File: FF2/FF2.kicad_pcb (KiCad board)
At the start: 2 copper layers, 140 x 140 mm, 80 parts, among them J1 AVR-ISP-6, SW1 RESET, SW2 BOOT, U1 ATmega328P-AU, Y1 16MHz

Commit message: updated switches footprints lib, start of placement on board
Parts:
- moved MX15 255.2 mm to (151.6, 132.1)
- moved DOB1 249.9 mm to (171.0, 132.1)
- moved H3 239.2 mm to (103.2, 156.0)
- moved MX20 238.4 mm to (190.5, 113.0)
- moved MX21 233.9 mm to (190.5, 132.2)
- moved H4 226.7 mm to (200.3, 156.0)
- moved MX19 220.7 mm to (190.5, 93.8)
- moved MX5 217.3 mm to (113.2, 132.1)
- moved MX10 216.6 mm to (132.4, 132.1)
- moved MX18 210.9 mm to (190.5, 74.6)
- moved MX17 204.9 mm to (190.4, 50.8)
- moved MX14 204.4 mm to (151.6, 112.9)
- moved MX3 181.4 mm to (113.2, 93.7)
- moved MX9 177.3 mm to (132.4, 112.9)
- moved MX4 156.6 mm to (113.2, 112.9)
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
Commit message: more component placement on the pcb
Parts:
- C1, C2, C3, C4, D1, D10, D11, D12, D13, D14, D15, D16, D17, D18, D19, D2, D20, D21, D3, D4, D5, D6, D7, D8, D9, DBA1, DBB1, DBC1, DBD1, DBP1, DM1, DM2, DR1, DR2, DZ1, DZ2, J1, R1, R2, R3, R4, R5, R6, R7, SW1, SW2, U1, Y1: moved to B.Cu
- moved DBP1 208.5 mm to (172.6, 143.3)
- moved D10 196.5 mm to (133.2, 122.5)
- moved DBB1 192.4 mm to (177.3, 143.3)
- moved D5 191.2 mm to (114.1, 122.5)
- moved DBD1 188.3 mm to (172.6, 121.8)
- moved DBA1 187.6 mm to (167.8, 143.3)
- moved D21 184.7 mm to (191.4, 122.7)
- moved DBC1 182.4 mm to (177.3, 121.8)
- moved DR2 180.5 mm to (176.5, 82.5)
- moved D20 163.6 mm to (191.3, 103.4)
- moved D14 158.4 mm to (152.5, 103.3)
- moved D15 155.0 mm to (152.4, 122.5)
- moved D9 154.2 mm to (133.2, 103.3)
- moved D19 152.7 mm to (191.3, 84.2)
- moved D4 150.6 mm to (114.1, 103.3)
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
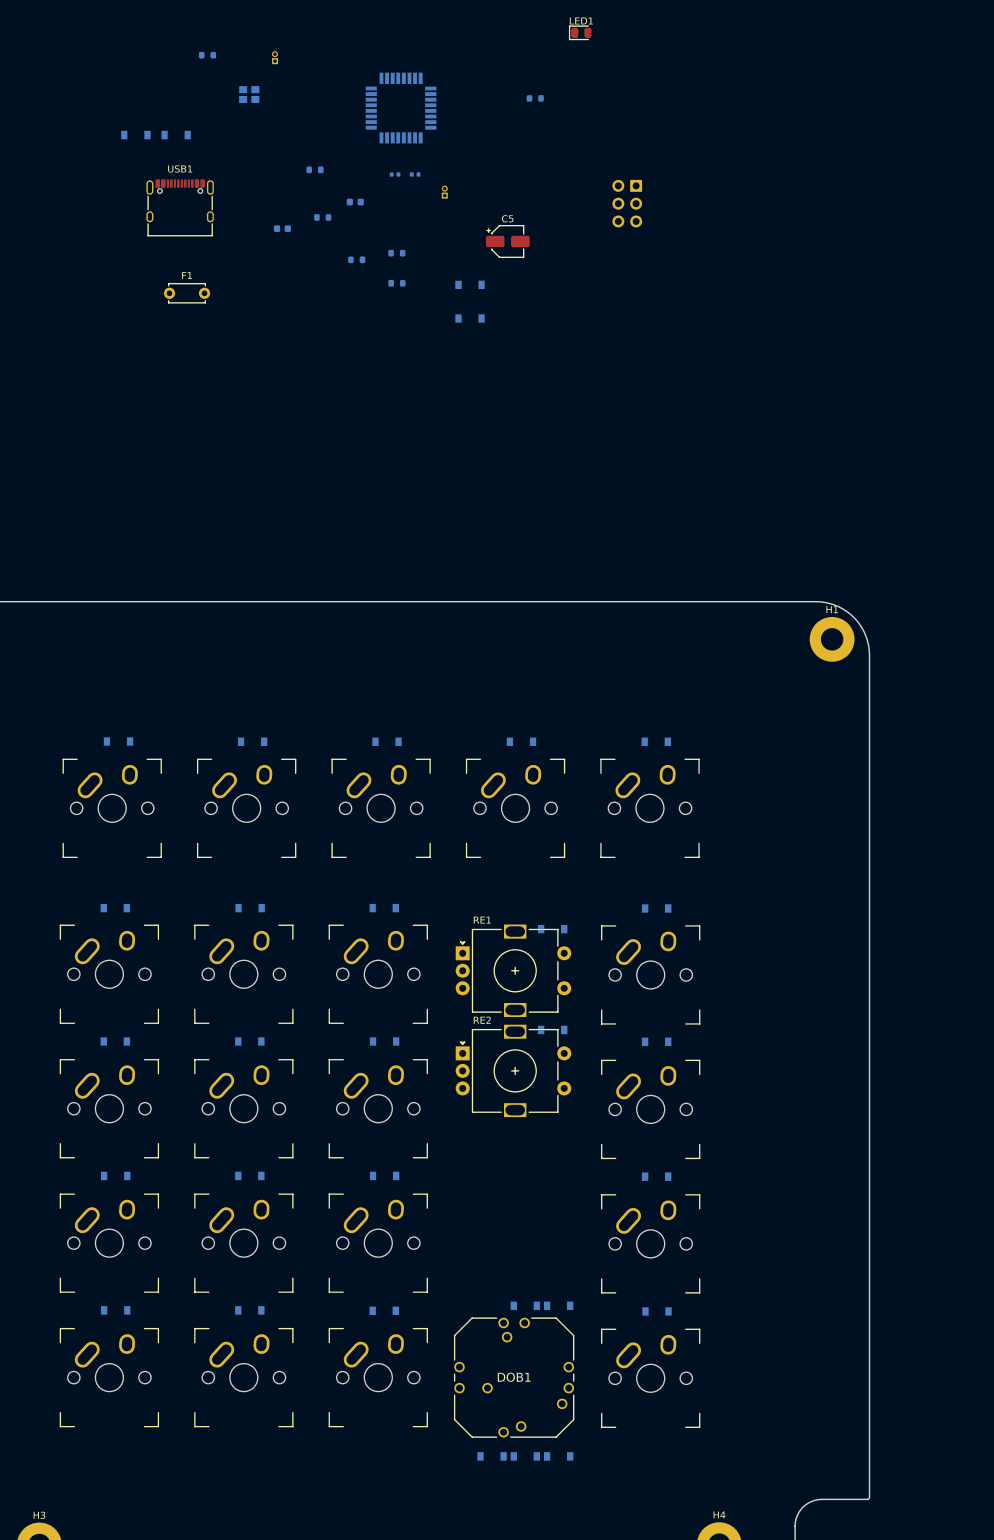
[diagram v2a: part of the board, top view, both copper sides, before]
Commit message: more routing, only dobber and 2-way missing
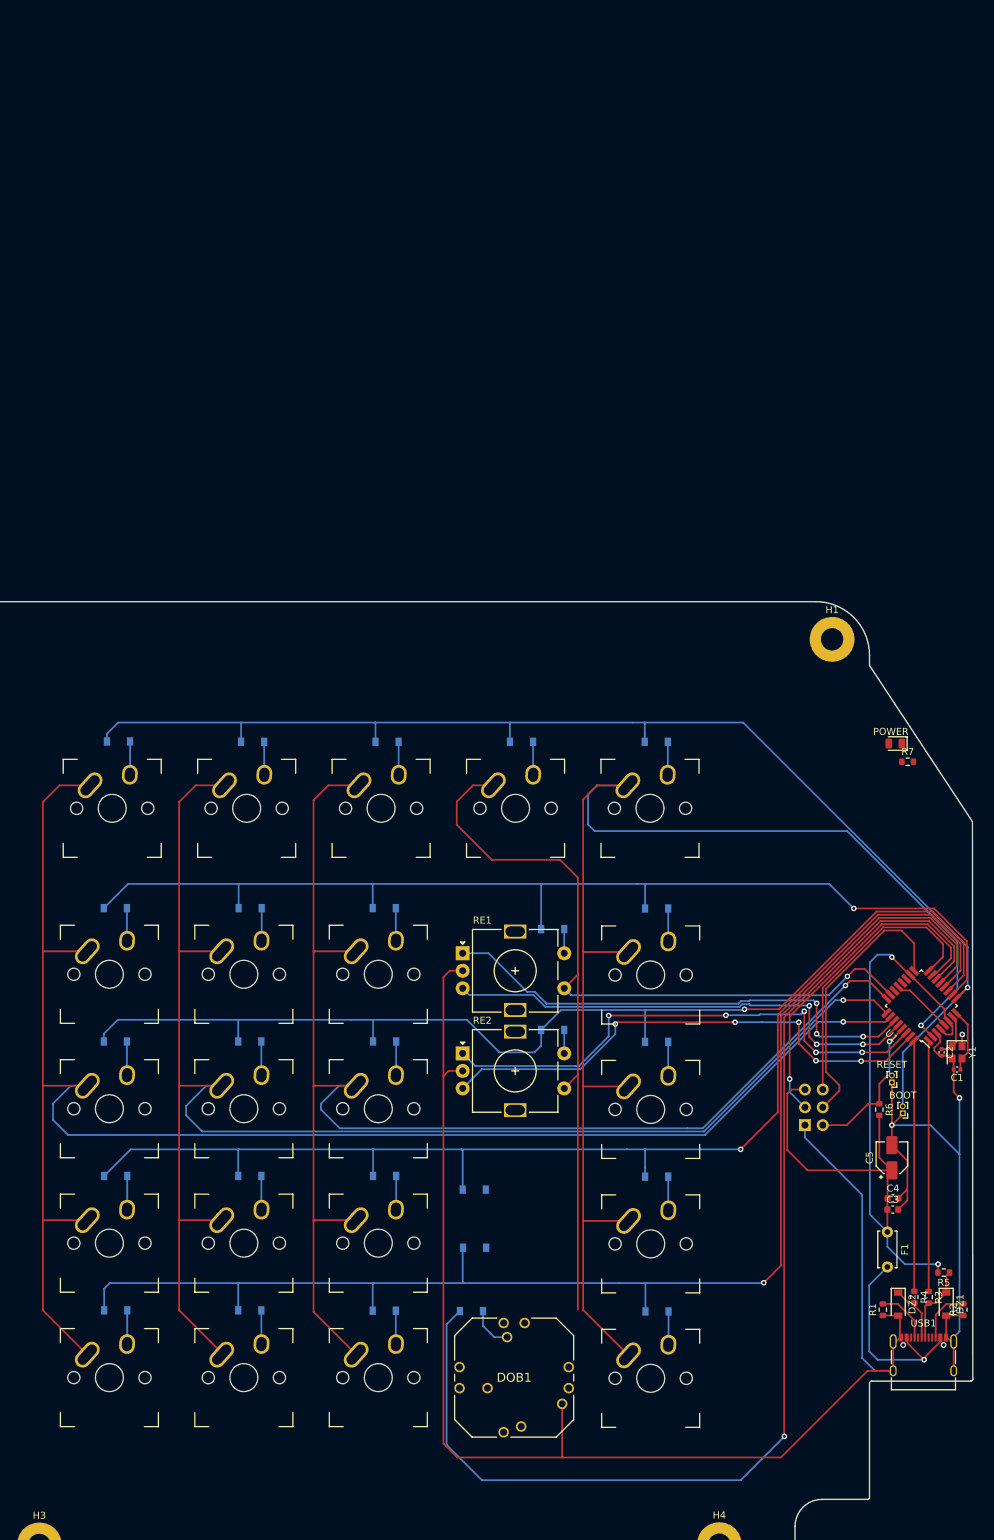
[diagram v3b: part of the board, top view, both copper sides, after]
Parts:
- removed DBA1, DBB1, DBC1, DBD1, DBP1: D_Small, Diode_SMD:D_SOD-123
- added DB1: D_Small, Diode_SMD:D_SOD-123, B.Cu at (164.9, 122.6)
- C1, C2, C3, C4, DZ1, DZ2, R1, R2, R3, R4, R5, R6, R7, SW1, SW2, U1, Y1: moved to F.Cu
- moved R1 203.5 mm to (223.7, 122.4), turned to 90 degrees
- moved DZ1 203.1 mm to (232.7, 121.6), turned to 270 degrees
- moved DZ2 196.2 mm to (225.8, 121.6), turned to 270 degrees
- moved USB1 196.0 mm to (229.4, 130.1)
- moved R5 181.3 mm to (232.3, 117.1), turned to 180 degrees
- moved R4 175.8 mm to (228.2, 120.6), turned to 270 degrees
- moved SW2 175.0 mm to (226.5, 94.3), turned to 180 degrees
- moved Y1 170.1 mm to (234.2, 85.7), turned to 270 degrees
- moved F1 168.8 mm to (224.3, 111.3), turned to 270 degrees
- moved R2 167.4 mm to (235.2, 122.4), turned to 90 degrees
- moved R3 167.3 mm to (230.2, 120.6), turned to 270 degrees
- moved C3 165.0 mm to (225.1, 108.1)
- moved C4 161.7 mm to (225.1, 106.5)
- moved C1 150.9 mm to (234.2, 88.1), turned to 180 degrees
- moved U1 148.2 mm to (229.2, 79.0), turned to 135 degrees
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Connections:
- D1 pad 1: ROW0 -> BOOT
- D11 pad 1: ROW0 -> BOOT
- D16 pad 1: ROW0 -> BOOT
- D17 pad 1: ROW0 -> BOOT
- D6 pad 1: ROW0 -> BOOT
- DOB1 pad 1: DOB1_A -> COL0
- DOB1 pad 11: DOB1_A -> COL3
- DOB1 pad 2: DOB1_P -> COL4
- DOB1 pad 4: DOB1_B -> COL1
- DOB1 pad 6: DOB1_C -> COL2
- DOB1 pad 7: COL4 -> DOB1_COM
- DOB1 pad 9: DOB1_A -> COL3
- MX17 pad 1: COL5 -> COL4
- MX18 pad 1: COL5 -> COL4
- MX19 pad 1: COL5 -> COL4
- MX20 pad 1: COL5 -> COL4
- MX21 pad 1: COL5 -> COL4
- U1 pad 10: Net-(U1-Pad10) -> ROW1
- U1 pad 11: Net-(U1-Pad11) -> ROW2
- U1 pad 12: Net-(U1-Pad12) -> ROW3
- U1 pad 13: Net-(U1-Pad13) -> ROW4
- U1 pad 14: Net-(U1-Pad14) -> ROW5
- U1 pad 2: Net-(U1-Pad2) -> COL4
- U1 pad 23: Net-(U1-Pad23) -> COL3
- U1 pad 24: Net-(U1-Pad24) -> COL2
- U1 pad 25: Net-(U1-Pad25) -> COL1
- U1 pad 26: Net-(U1-Pad26) -> COL0
- U1 pad 27: Net-(U1-Pad27) -> R1A
- U1 pad 28: Net-(U1-Pad28) -> R1B
- U1 pad 30: Net-(U1-Pad30) -> R2A
- U1 pad 31: Net-(U1-Pad31) -> R2B
- U1 pad 9: Net-(U1-Pad9) -> BOOT
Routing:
- net GND: track 0.00 -> 307.5 mm, vias 0 -> 3
- net COL0: track 0.00 -> 244.1 mm, vias 0 -> 1
- net COL1: track 0.00 -> 224.3 mm, vias 0 -> 1
- net COL2: track 0.00 -> 206.0 mm, vias 0 -> 1
- net COL4: track 0.00 -> 195.5 mm, vias 0 -> 1
- net ROW4: track 0.00 -> 193.2 mm, vias 0 -> 1
- net BOOT: track 0.00 -> 177.9 mm, vias 0 -> 1
- net ROW3: track 0.00 -> 172.0 mm, vias 0 -> 1
- net ROW5: track 0.00 -> 169.9 mm, vias 0 -> 1
- net ROW2: track 0.00 -> 156.7 mm, vias 0 -> 1
- net ROW1: track 0.00 -> 153.5 mm, vias 0 -> 1
- net COL3: track 0.00 -> 147.2 mm, vias 0 -> 1
- net +5V: track 0.00 -> 117.0 mm, vias 0 -> 2
- net R2A: track 0.00 -> 75.1 mm, vias 0 -> 5
- net R2B: track 0.00 -> 74.2 mm, vias 0 -> 5
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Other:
- board size 140 x 140 mm -> 154.8 x 140 mm

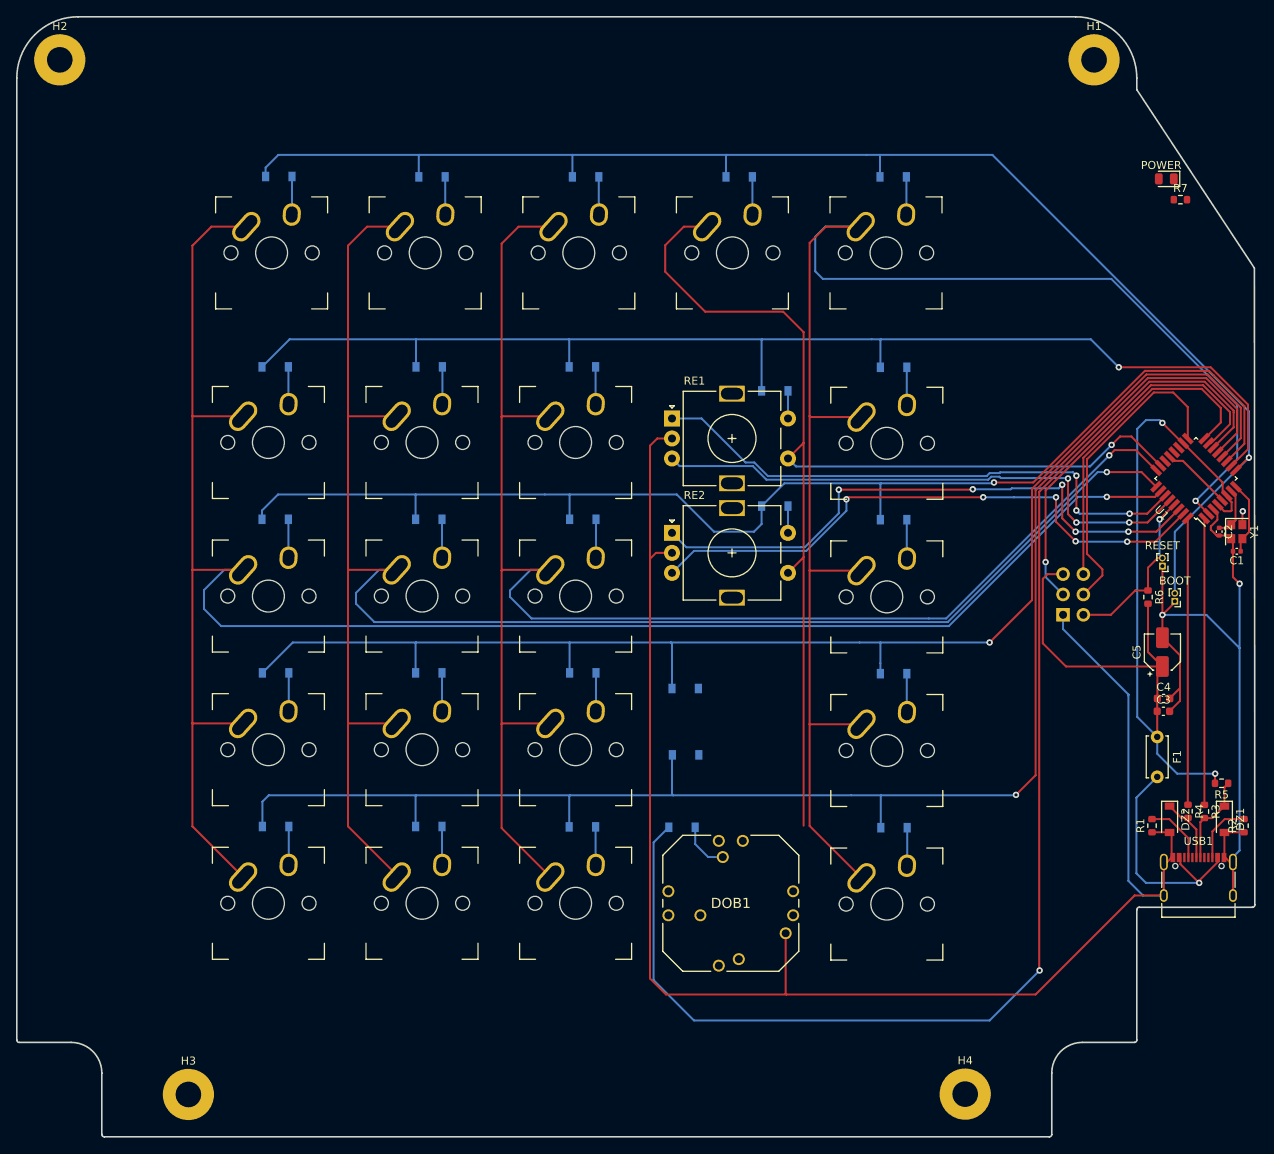
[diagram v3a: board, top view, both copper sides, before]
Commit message: updated with all SMD on the front and part numbers for production
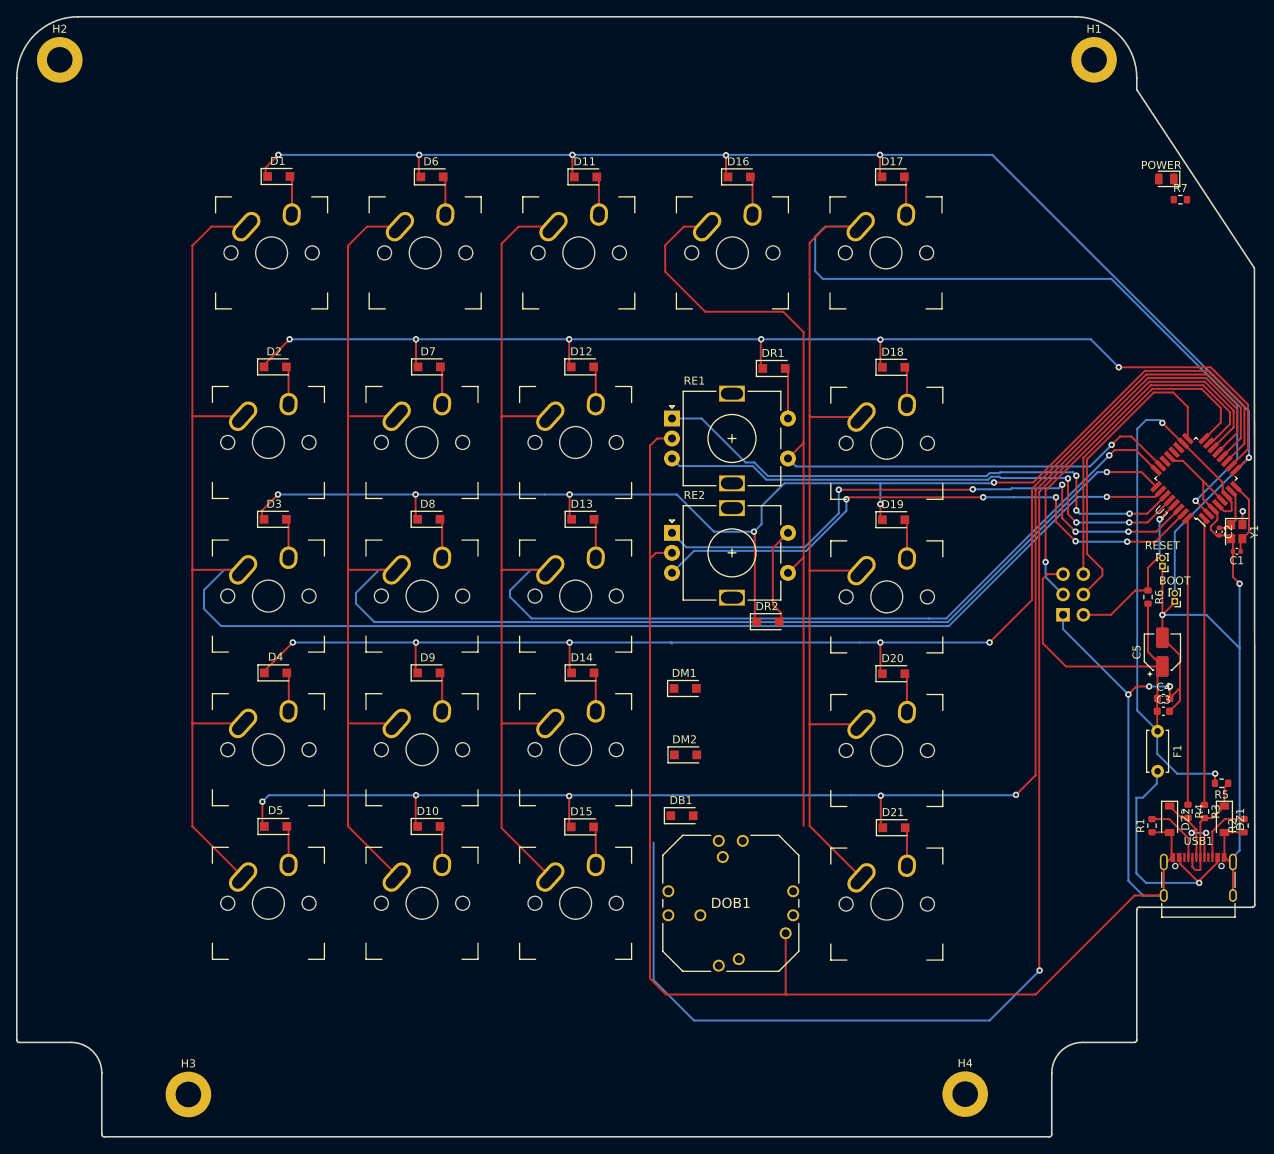
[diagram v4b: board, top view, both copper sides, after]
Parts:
- D1, D10, D11, D12, D13, D14, D15, D16, D17, D18, D19, D2, D20, D21, D3, D4, D5, D6, D7, D8, D9, DB1, DM1, DM2, DR1, DR2: footprint Diode_SMD:D_SOD-123 -> Diode_SMD:D_SOD-123F; moved to F.Cu
- H1, H2, H3, H4: footprint MountingHole:MountingHole_3.2mm_M3_Pad -> MountingHole:MountingHole_3.2mm_M3_ISO7380_Pad
- moved DR2 14.5 mm to (175.7, 96.9)
- moved DR1 2.80 mm to (176.4, 65.2)
- moved DB1 1.45 mm to (164.9, 121.2)
- moved F1 0.70 mm to (224.3, 110.6)
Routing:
- net GND: track 307.5 -> 319.3 mm, vias 3 -> 6
- net ROW2: track 156.7 -> 168.0 mm, vias 1 -> 6
- net RE2_S: track 3.35 -> 12.3 mm
- net DOB1_COM: track 6.22 -> 0.00 mm
- net Net-(DZ2-Pad1): track 8.30 -> 14.1 mm, vias 0 -> 2
- net ROW3: track 172.0 -> 166.5 mm, vias 1 -> 5
- net ROW4: track 193.2 -> 187.8 mm, vias 1 -> 5
- net Net-(DZ1-Pad1): track 11.3 -> 15.2 mm
- net RE1_S: track 3.45 -> 6.29 mm
- net ROW1: track 153.5 -> 150.7 mm, vias 1 -> 6
- net ROW5: track 169.9 -> 167.2 mm
- net VCC: track 29.8 -> 31.6 mm
- net +5V: track 117.0 -> 115.4 mm
- net BOOT: vias 1 -> 6
